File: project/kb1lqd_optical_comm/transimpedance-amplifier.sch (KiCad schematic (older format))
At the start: 10 parts

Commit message: Schematic essentially done.
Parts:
- removed C?: 1uF, symbol Device:C
- removed RV?: 1MEG, symbol Device:R_POT
- added C11: 1uF, symbol Device:C
- C9: renamed from C?; value 10nF -> 100nF
- D2: renamed from D?; value D_Photo -> ODD-1W
- R27: renamed from R?; value 250k -> 500k
- gave numbers to parts that had none: 5
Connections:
- wire segments 34 -> 32
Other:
- note added: "Id(Max) Expected 2uA"
- note added: "Vbias=2.5V"
- note added: "Vout expected to be maximum of 1Vp-p"
- note added: "WARNING: Vout contains 2.5V DC bias!"
- moved on the sheet: C8, C9, D2, R25, R26

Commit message: Updated with all footprints
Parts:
- C10: footprint (none) -> Capacitor_SMD:C_0603_1608Metric
- C11: footprint (none) -> Capacitor_SMD:C_1206_3216Metric
- C8, C9: footprint (none) -> Capacitor_SMD:C_0805_2012Metric
- D2: footprint (none) -> Package_TO_SOT_THT:TO-18-2
- R25, R26, R27: footprint (none) -> Resistor_SMD:R_0603_1608Metric
- U3: footprint (none) -> Package_SO:SOIC-8_3.9x4.9mm_P1.27mm
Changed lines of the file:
@@
 F 0 "U3" H 5844 4546 50  0000 L CNN
 F 1 "ADA4610-1" H 5844 4455 50  0000 L CNN
-F 2 "" H 5450 4200 50  0001 C CNN
+F 2 "Package_SO:SOIC-8_3.9x4.9mm_P1.27mm" H 5450 4200 50  0001 C CNN
 F 3 "" H 5450 4200 50  0001 C CNN
 	1    5450 4200
@@
 F 0 "R27" V 5595 3450 50  0000 C CNN
 F 1 "500k" V 5686 3450 50  0000 C CNN
-F 2 "" V 5840 3440 50  0001 C CNN
+F 2 "Resistor_SMD:R_0603_1608Metric" V 5840 3440 50  0001 C CNN
 F 3 "~" H 5800 3450 50  0001 C CNN
 	1    5800 3450
@@
 F 0 "R25" H 4668 3396 50  0000 L CNN
 F 1 "10k" H 4668 3305 50  0000 L CNN
-F 2 "" V 4640 3340 50  0001 C CNN
+F 2 "Resistor_SMD:R_0603_1608Metric" V 4640 3340 50  0001 C CNN
 F 3 "~" H 4600 3350 50  0001 C CNN
 	1    4600 3350
@@
 F 0 "R26" H 4668 4596 50  0000 L CNN
 F 1 "10k" H 4668 4505 50  0000 L CNN
-F 2 "" V 4640 4540 50  0001 C CNN
+F 2 "Resistor_SMD:R_0603_1608Metric" V 4640 4540 50  0001 C CNN
 F 3 "~" H 4600 4550 50  0001 C CNN
 	1    4600 4550
@@
 F 0 "C9" H 5715 2246 50  0000 L CNN
 F 1 "100nF" H 5715 2155 50  0000 L CNN
-F 2 "" H 5638 2050 50  0001 C CNN
+F 2 "Capacitor_SMD:C_0805_2012Metric" H 5638 2050 50  0001 C CNN
 F 3 "~" H 5600 2200 50  0001 C CNN
 	1    5600 2200
@@
 F 0 "C8" H 4265 4596 50  0000 L CNN
 F 1 "6.8nF" H 4265 4505 50  0000 L CNN
-F 2 "" H 4188 4400 50  0001 C CNN
+F 2 "Capacitor_SMD:C_0805_2012Metric" H 4188 4400 50  0001 C CNN
 F 3 "~" H 4150 4550 50  0001 C CNN
 	1    4150 4550
@@
 F 0 "C10" V 5548 3050 50  0000 C CNN
 F 1 "33pF" V 5650 3050 50  0000 C CNN
-F 2 "" H 5838 2900 50  0001 C CNN
+F 2 "Capacitor_SMD:C_0603_1608Metric" H 5838 2900 50  0001 C CNN
 F 3 "~" H 5800 3050 50  0001 C CNN
 	1    5800 3050
@@
 F 0 "D2" V 3004 4558 50  0000 L CNN
 F 1 "ODD-1W" V 3095 4558 50  0000 L CNN
-F 2 "" H 3050 4400 50  0001 C CNN
+F 2 "Package_TO_SOT_THT:TO-18-2" H 3050 4400 50  0001 C CNN
 F 3 "~" H 3050 4400 50  0001 C CNN
 	1    3100 4400
@@
 F 0 "C11" H 6265 2246 50  0000 L CNN
 F 1 "1uF" H 6265 2155 50  0000 L CNN
-F 2 "" H 6188 2050 50  0001 C CNN
+F 2 "Capacitor_SMD:C_1206_3216Metric" H 6188 2050 50  0001 C CNN
 F 3 "~" H 6150 2200 50  0001 C CNN
 	1    6150 2200

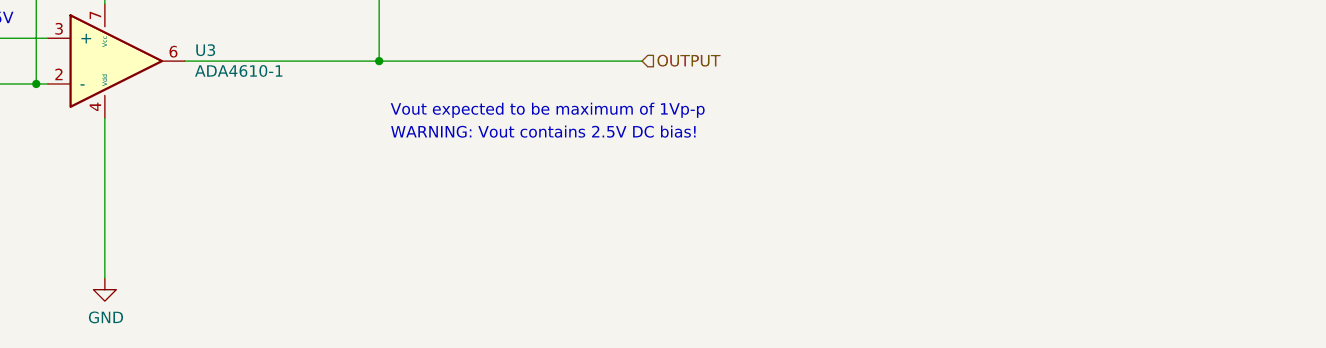
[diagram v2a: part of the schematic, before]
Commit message: Fixed a few errors in silkscreen, found an open item error in U3 generated footprint.
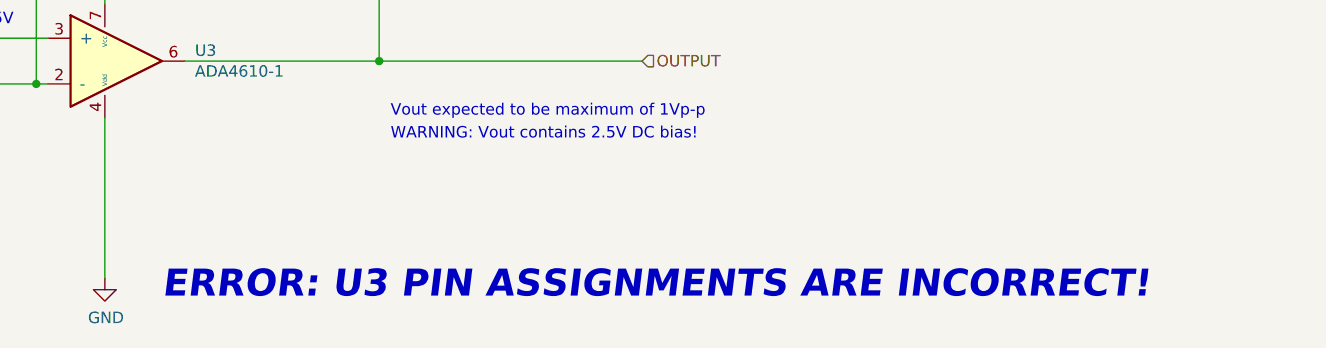
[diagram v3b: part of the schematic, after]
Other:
- note added: "ERROR: U3 PIN ASSIGNMENTS ARE INCORRECT!"
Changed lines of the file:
@@
 Text Notes 6700 4250 0    50   ~ 0
 WARNING: Vout contains 2.5V DC bias!
+Text Notes 5700 4950 0    118  Italic 24
+ERROR: U3 PIN ASSIGNMENTS ARE INCORRECT!
 $EndSCHEMATC
